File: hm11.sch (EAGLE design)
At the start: 2 parts

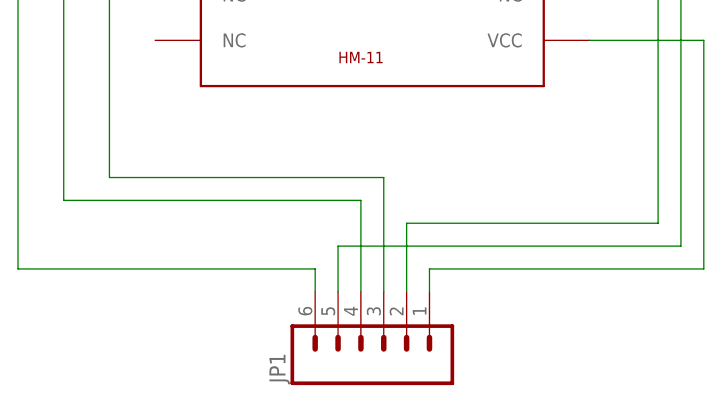
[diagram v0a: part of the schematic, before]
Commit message: Reduced size of board, cleaned up connections
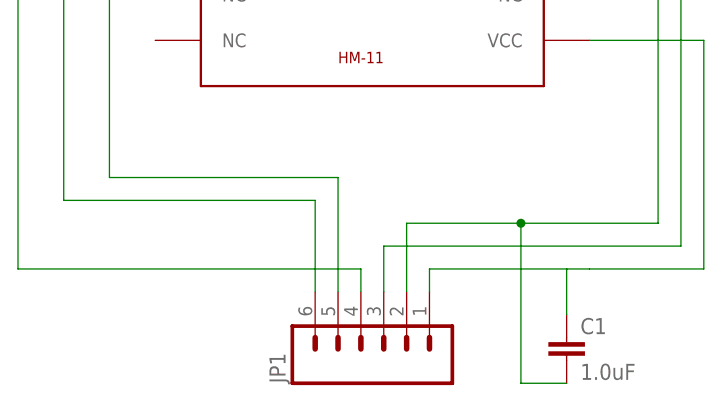
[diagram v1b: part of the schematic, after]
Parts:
- added C1: 1.0uF, SparkFun-Capacitors:1.0UF-0603-16V-10%
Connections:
- net GND: now also C1.2
- net N$2: now also C1.1
- net N$3: now also JP1.5; no longer JP1.3
- net N$4: now also JP1.4; no longer JP1.6
- net N$5: now also JP1.6; no longer JP1.4
- net N$6: now also JP1.3; no longer JP1.5
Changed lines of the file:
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@@
 <?xml version="1.0" encoding="utf-8"?>
 <!DOCTYPE eagle SYSTEM "eagle.dtd">
-<eagle version="7.2.0">
+<eagle version="7.7.0">
 <drawing>
 <settings>
@@
 <layer number="54" name="bGND_GNDA" color="1" fill="9" visible="no" active="no"/>
 <layer number="56" name="wert" color="7" fill="1" visible="no" active="no"/>
+<layer number="57" name="tCAD" color="7" fill="1" visible="no" active="no"/>
+<layer number="59" name="tCarbon" color="7" fill="1" visible="no" active="no"/>
+<layer number="60" name="bCarbon" color="7" fill="1" visible="no" active="no"/>
+<layer number="90" name="Modules" color="5" fill="1" visible="yes" active="yes"/>
 <layer number="91" name="Nets" color="2" fill="1" visible="yes" active="yes"/>
 <layer number="92" name="Busses" color="1" fill="1" visible="yes" active="yes"/>
@@
 <layer number="97" name="Info" color="7" fill="1" visible="yes" active="yes"/>
 <layer number="98" name="Guide" color="6" fill="1" visible="yes" active="yes"/>
+<layer number="99" name="SpiceOrder" color="7" fill="1" visible="yes" active="yes"/>
 <layer number="100" name="Muster" color="7" fill="1" visible="no" active="no"/>
 <layer number="101" name="Patch_Top" color="12" fill="4" visible="yes" active="yes"/>
@@
 <layer number="108" name="tplace-old" color="10" fill="1" visible="yes" active="yes"/>
 <layer number="109" name="ref-old" color="11" fill="1" visible="yes" active="yes"/>
+<layer number="110" name="fp0" color="7" fill="1" visible="yes" active="yes"/>
+<layer number="111" name="LPC17xx" color="7" fill="1" visible="yes" active="yes"/>
+<layer number="112" name="tSilk" color="7" fill="1" visible="yes" active="yes"/>
+<layer number="113" name="IDFDebug" color="7" fill="1" visible="yes" active="yes"/>
+<layer number="114" name="Badge_Outline" color="7" fill="1" visible="yes" active="yes"/>
+<layer number="115" name="ReferenceISLANDS" color="7" fill="1" visible="yes" active="yes"/>
 <layer number="116" name="Patch_BOT" color="9" fill="4" visible="yes" active="yes"/>
+<layer number="118" name="Rect_Pads" color="7" fill="1" visible="yes" active="yes"/>
 <layer number="121" name="_tsilk" color="7" fill="1" visible="yes" active="yes"/>
 <layer number="122" name="_bsilk" color="7" fill="1" visible="yes" active="yes"/>
+<layer number="123" name="tTestmark" color="7" fill="1" visible="yes" active="yes"/>
+<layer number="124" name="bTestmark" color="7" fill="1" visible="yes" active="yes"/>
 <layer number="125" name="_tNames" color="7" fill="1" visible="yes" active="yes"/>
+<layer number="126" name="_bNames" color="7" fill="1" visible="yes" active="yes"/>
+<layer number="127" name="_tValues" color="7" fill="1" visible="yes" active="yes"/>
+<layer number="128" name="_bValues" color="7" fill="1" visible="yes" active="yes"/>
+<layer number="129" name="Mask" color="7" fill="1" visible="yes" active="yes"/>
+<layer number="131" name="tAdjust" color="7" fill="1" visible="yes" active="yes"/>
+<layer number="132" name="bAdjust" color="7" fill="1" visible="yes" active="yes"/>
 <layer number="144" name="Drill_legend" color="7" fill="1" visible="yes" active="yes"/>
+<layer number="150" name="Notes" color="7" fill="1" visible="yes" active="yes"/>
 <layer number="151" name="HeatSink" color="7" fill="1" visible="yes" active="yes"/>
+<layer number="152" name="_bDocu" color="7" fill="1" visible="yes" active="yes"/>
+<layer number="153" name="FabDoc1" color="7" fill="1" visible="yes" active="yes"/>
+<layer number="154" name="FabDoc2" color="7" fill="1" visible="yes" active="yes"/>
+<layer number="155" name="FabDoc3" color="7" fill="1" visible="yes" active="yes"/>
 <layer number="199" name="Contour" color="7" fill="1" visible="yes" active="yes"/>
 <layer number="200" name="200bmp" color="1" fill="10" visible="yes" active="yes"/>
@@
 <layer number="223" name="223bmp" color="24" fill="1" visible="no" active="no"/>
 <layer number="224" name="224bmp" color="25" fill="1" visible="no" active="no"/>
+<layer number="225" name="225bmp" color="7" fill="1" visible="yes" active="yes"/>
+<layer number="226" name="226bmp" color="7" fill="1" visible="yes" active="yes"/>
+<layer number="227" name="227bmp" color="7" fill="1" visible="yes" active="yes"/>
+<layer number="228" name="228bmp" color="7" fill="1" visible="yes" active="yes"/>
+<layer number="229" name="229bmp" color="7" fill="1" visible="yes" active="yes"/>
+<layer number="230" name="230bmp" color="7" fill="1" visible="yes" active="yes"/>
+<layer number="231" name="231bmp" color="7" fill="1" visible="yes" active="yes"/>
+<layer number="248" name="Housing" color="7" fill="1" visible="yes" active="yes"/>
+<layer number="249" name="Edge" color="7" fill="1" visible="yes" active="yes"/>
 <layer number="250" name="Descript" color="3" fill="1" visible="no" active="no"/>
 <layer number="251" name="SMDround" color="12" fill="11" visible="no" active="no"/>
 <layer number="254" name="cooling" color="7" fill="1" visible="yes" active="yes"/>
+<layer number="255" name="routoute" color="7" fill="1" visible="yes" active="yes"/>
 </layers>
 <schematic xreflabel="%F%N/%S.%C%R" xrefpart="/%S.%C%R">
@@
 <part name="U$1" library="hm-11" deviceset="HM-11" device=""/>
 <part name="JP1" library="SparkFun-Connectors" deviceset="M06" device="SIP"/>
+<part name="C1" library="SparkFun-Capacitors" deviceset="1.0UF" device="-0603-16V-10%" value="1.0uF"/>
 </parts>
 <sheets>
@@
 <instance part="U$1" gate="G$1" x="68.58" y="45.72"/>
 <instance part="JP1" gate="G$1" x="71.12" y="-5.08" rot="R90"/>
+<instance part="C1" gate="G$1" x="91.44" y="-7.62"/>
 </instances>
 <busses>
@@
 <wire x1="106.68" y1="76.2" x2="30.48" y2="76.2" width="0.1524" layer="91"/>
 <wire x1="30.48" y1="76.2" x2="30.48" y2="2.54" width="0.1524" layer="91"/>
-<pinref part="JP1" gate="G$1" pin="6"/>
-<wire x1="30.48" y1="2.54" x2="63.5" y2="2.54" width="0.1524" layer="91"/>
-<wire x1="63.5" y1="2.54" x2="63.5" y2="0" width="0.1524" layer="91"/>
+<wire x1="30.48" y1="2.54" x2="68.58" y2="2.54" width="0.1524" layer="91"/>
+<pinref part="JP1" gate="G$1" pin="4"/>
+<wire x1="68.58" y1="0" x2="68.58" y2="2.54" width="0.1524" layer="91"/>
 </segment>
 </net>
@@
 <wire x1="106.68" y1="27.94" x2="106.68" y2="2.54" width="0.1524" layer="91"/>
 <pinref part="JP1" gate="G$1" pin="1"/>
-<wire x1="106.68" y1="2.54" x2="76.2" y2="2.54" width="0.1524" layer="91"/>
+<wire x1="106.68" y1="2.54" x2="93.98" y2="2.54" width="0.1524" layer="91"/>
+<wire x1="91.44" y1="2.54" x2="76.2" y2="2.54" width="0.1524" layer="91"/>
 <wire x1="76.2" y1="2.54" x2="76.2" y2="0" width="0.1524" layer="91"/>
+<pinref part="C1" gate="G$1" pin="1"/>
+<wire x1="93.98" y1="2.54" x2="91.44" y2="2.54" width="0.1524" layer="91"/>
+<wire x1="91.44" y1="2.54" x2="91.44" y2="-2.54" width="0.1524" layer="91"/>
 </segment>
 </net>
@@
 <wire x1="93.98" y1="38.1" x2="104.14" y2="38.1" width="0.1524" layer="91"/>
 <wire x1="104.14" y1="38.1" x2="104.14" y2="5.08" width="0.1524" layer="91"/>
-<pinref part="JP1" gate="G$1" pin="5"/>
-<wire x1="104.14" y1="5.08" x2="66.04" y2="5.08" width="0.1524" layer="91"/>
-<wire x1="66.04" y1="5.08" x2="66.04" y2="0" width="0.1524" layer="91"/>
+<wire x1="104.14" y1="5.08" x2="71.12" y2="5.08" width="0.1524" layer="91"/>
+<pinref part="JP1" gate="G$1" pin="3"/>
+<wire x1="71.12" y1="0" x2="71.12" y2="5.08" width="0.1524" layer="91"/>
 </segment>
 </net>
@@
 <wire x1="93.98" y1="43.18" x2="101.6" y2="43.18" width="0.1524" layer="91"/>
 <wire x1="101.6" y1="43.18" x2="101.6" y2="7.62" width="0.1524" layer="91"/>
-<wire x1="101.6" y1="7.62" x2="73.66" y2="7.62" width="0.1524" layer="91"/>
+<wire x1="101.6" y1="7.62" x2="86.36" y2="7.62" width="0.1524" layer="91"/>
 <pinref part="JP1" gate="G$1" pin="2"/>
+<wire x1="86.36" y1="7.62" x2="73.66" y2="7.62" width="0.1524" layer="91"/>
 <wire x1="73.66" y1="7.62" x2="73.66" y2="0" width="0.1524" layer="91"/>
+<pinref part="C1" gate="G$1" pin="2"/>
+<wire x1="91.44" y1="-10.16" x2="86.36" y2="-10.16" width="0.1524" layer="91"/>
+<wire x1="86.36" y1="-10.16" x2="86.36" y2="7.62" width="0.1524" layer="91"/>
+<junction x="86.36" y="7.62"/>
 </segment>
 </net>
@@
 <wire x1="45.72" y1="58.42" x2="40.64" y2="58.42" width="0.1524" layer="91"/>
 <wire x1="40.64" y1="58.42" x2="40.64" y2="12.7" width="0.1524" layer="91"/>
-<wire x1="40.64" y1="12.7" x2="71.12" y2="12.7" width="0.1524" layer="91"/>
-<pinref part="JP1" gate="G$1" pin="3"/>
-<wire x1="71.12" y1="12.7" x2="71.12" y2="0" width="0.1524" layer="91"/>
+<wire x1="40.64" y1="12.7" x2="66.04" y2="12.7" width="0.1524" layer="91"/>
+<pinref part="JP1" gate="G$1" pin="5"/>
+<wire x1="66.04" y1="0" x2="66.04" y2="12.7" width="0.1524" layer="91"/>
 </segment>
 </net>
@@
 <wire x1="45.72" y1="48.26" x2="35.56" y2="48.26" width="0.1524" layer="91"/>
 <wire x1="35.56" y1="48.26" x2="35.56" y2="10.16" width="0.1524" layer="91"/>
-<wire x1="35.56" y1="10.16" x2="68.58" y2="10.16" width="0.1524" layer="91"/>
-<pinref part="JP1" gate="G$1" pin="4"/>
-<wire x1="68.58" y1="10.16" x2="68.58" y2="0" width="0.1524" layer="91"/>
-</segment>
-</net>
+<wire x1="35.56" y1="10.16" x2="63.5" y2="10.16" width="0.1524" layer="91"/>
+<pinref part="JP1" gate="G$1" pin="6"/>
+<wire x1="63.5" y1="0" x2="63.5" y2="10.16" width="0.1524" layer="91"/>
+</segment>
+</net>
